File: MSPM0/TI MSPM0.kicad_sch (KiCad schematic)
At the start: 30 parts, among them J1 USB_C 4105-GF-A, J2 Conn_ARM_SWD_TagConnect_TC2030, U1 MSPM0G3507SPTR, U2 USBLC6-2SC6, U3 SPX3819M5-L-3-3, U4 CH340E, U5 LIS2DH, X1 8MHz

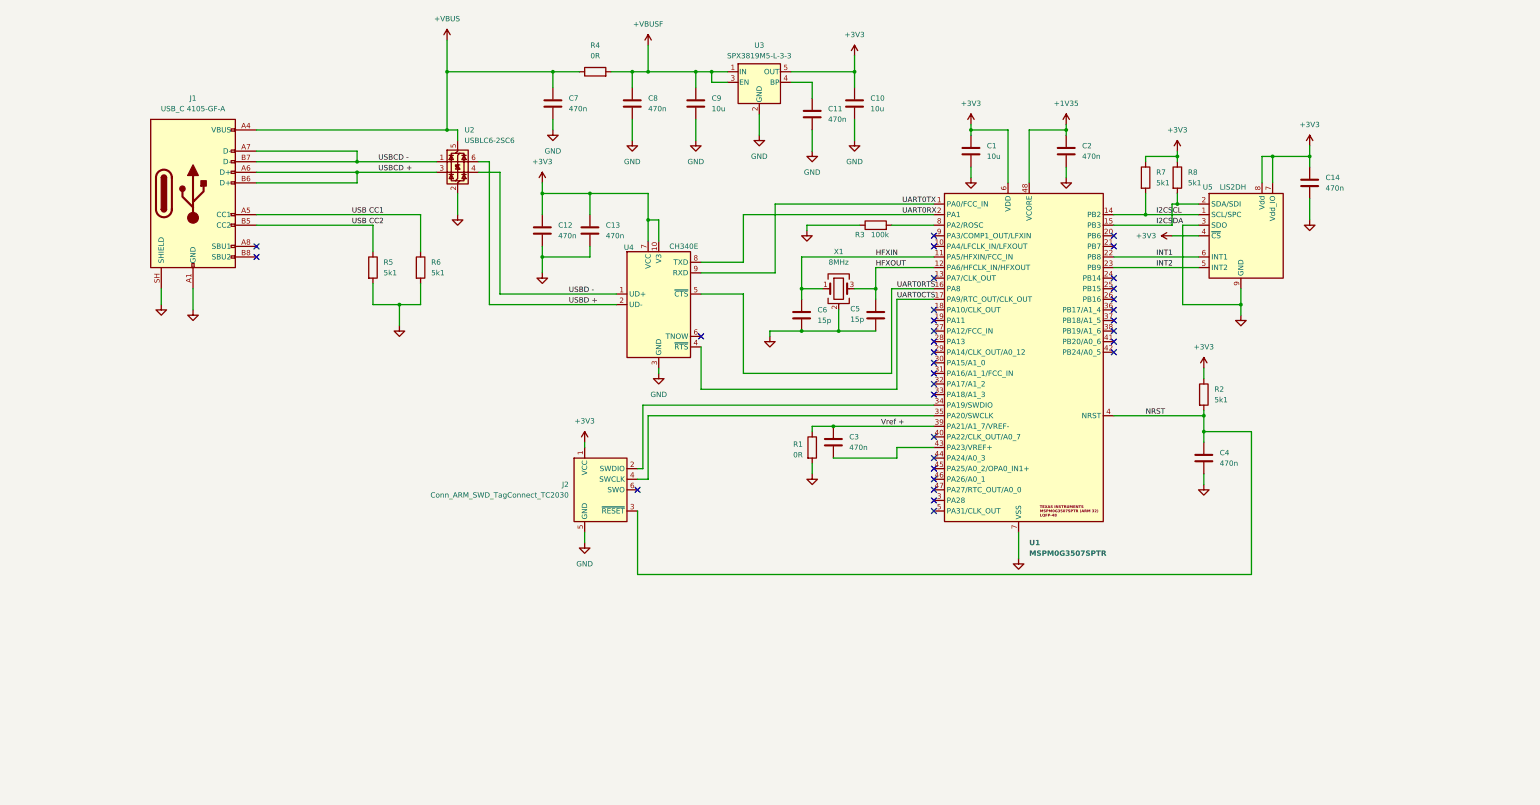
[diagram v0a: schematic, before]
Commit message: sch cleanup, added net classes
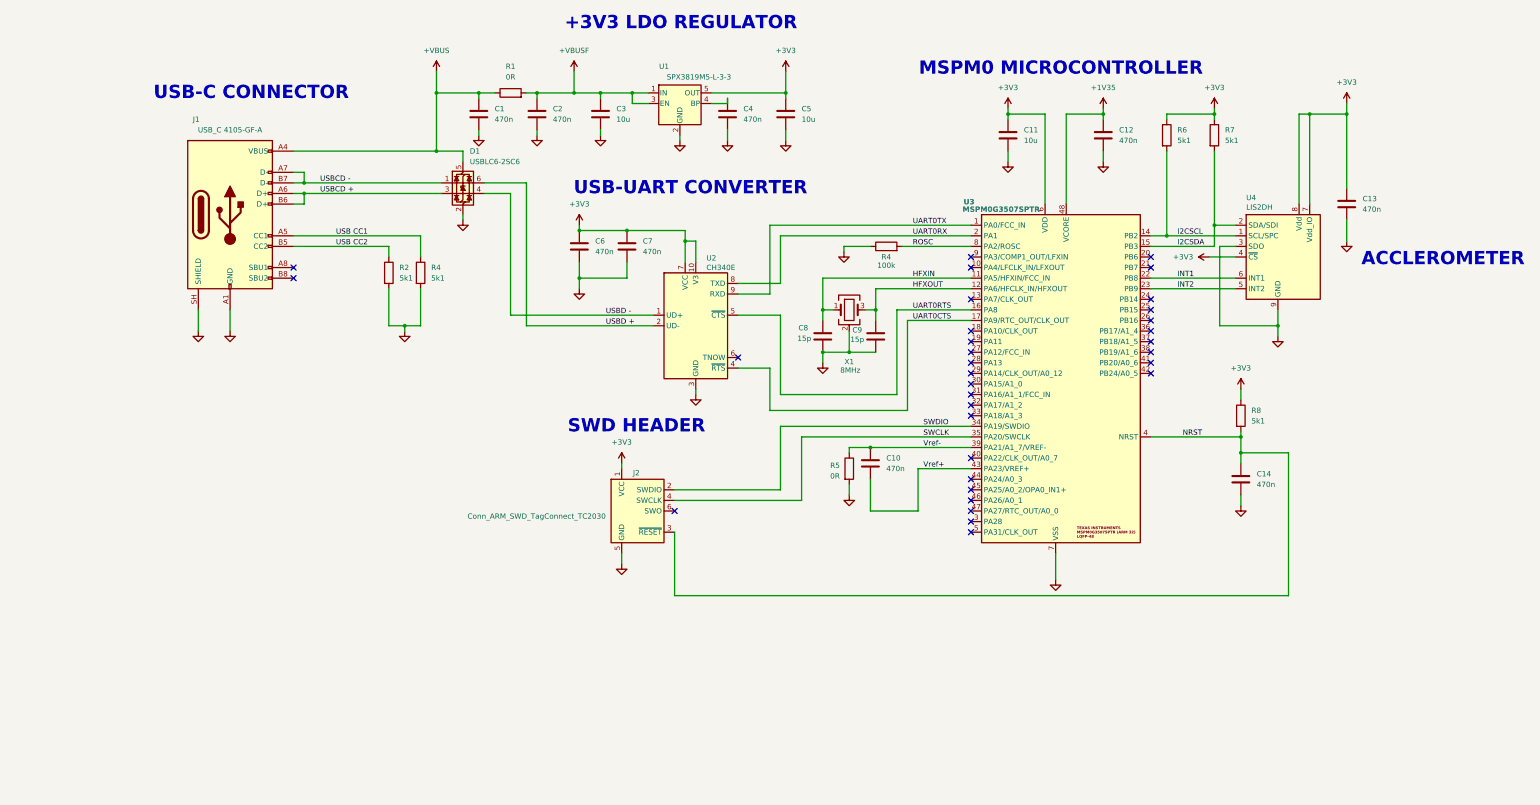
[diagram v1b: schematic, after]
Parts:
- renumbered C7 to C1, C3 to C10, C1 to C11, C2 to C12, C14 to C13, C4 to C14, C8 to C2, C9 to C3, C11 to C4, C10 to C5, C12 to C6, C13 to C7, C6 to C8, C5 to C9, U2 to D1, R4 to R1, R5 to R2, R6 to R4, R3 to R4, R1 to R5, R7 to R6, R8 to R7, R2 to R8, U3 to U1, U4 to U2, U1 to U3, U5 to U4
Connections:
- net Vref+: now reaches C10.2, U3.43 (PA23/VREF+)
- net SWDIO: now reaches J2.2 (SWDIO), U3.34 (PA19/SWDIO)
- net SWCLK: now reaches J2.4 (SWCLK), U3.35 (PA20/SWCLK)
- net ROSC: now reaches R4.2, U3.8 (PA2/ROSC)
- net Vref + renamed Vref-
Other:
- note added: "+3V3 LDO REGULATOR"
- note added: "ACCLEROMETER"
- note added: "MSPM0 MICROCONTROLLER"
- note added: "SWD HEADER"
- note added: "USB-C CONNECTOR"
- note added: "USB-UART CONVERTER"
- moved on the sheet: C1, C10, C11, C12, C13, C14, C2, C3, C4, C5, C6, C7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

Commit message: added mounting holes and fiducils
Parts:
- added FID1, FID2, FID3: Fiducial, symbol Mechanical:Fiducial
- added MH1, MH2, MH3 (x2): MountingHole_Pad, MountingHole:MountingHole_3.2mm_M3_Pad_Via, symbol Mechanical:MountingHole_Pad
- renumbered R4 to R3
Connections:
- net GND: now also MH1.1, MH2.1, MH3.1, MH3.1
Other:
- moved on the sheet: C4

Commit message: added components to layout
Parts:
- FID1, FID2, FID3: footprint (none) -> Fiducial:Fiducial_1mm_Mask2mm
- renumbered MH3 to MH4
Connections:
- net USBD +: now also D1.4 (I/O2), U2.1 (UD+); no longer D1.6 (I/O1), U2.2 (UD-)
- net USBD -: now also D1.6 (I/O1), U2.2 (UD-); no longer D1.4 (I/O2), U2.1 (UD+)
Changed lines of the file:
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@@
 		)
 	)
-	(label "USBD -"
+	(label "USBD +"
 		(at 176.53 130.81 0)
 		(effects
@@
 		)
 	)
-	(label "USBD +"
+	(label "USBD -"
 		(at 176.53 133.35 0)
 		(effects
@@
 		(dnp no)
 		(fields_autoplaced yes)
-		(property "Reference" "MH3"
+		(property "Reference" "MH4"
 			(at 111.76 224.7899 0)
 			(show_name no)
@@
 			(project "TI MSPM0"
 				(path "/afd132a1-7bf8-491c-b5ec-f7b4c9d34512"
-					(reference "MH3")
+					(reference "MH4")
 					(unit 1)
 				)
@@
 			)
 		)
-		(property "Footprint" ""
+		(property "Footprint" "Fiducial:Fiducial_1mm_Mask2mm"
 			(at 177.8 227.33 0)
 			(hide yes)
@@
 			)
 		)
-		(property "Footprint" ""
+		(property "Footprint" "Fiducial:Fiducial_1mm_Mask2mm"
 			(at 191.77 227.33 0)
 			(hide yes)
@@
 			)
 		)
-		(property "Footprint" ""
+		(property "Footprint" "Fiducial:Fiducial_1mm_Mask2mm"
 			(at 163.83 227.33 0)
 			(hide yes)
